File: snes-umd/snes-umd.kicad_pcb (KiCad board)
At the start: 2 copper layers, 2 parts

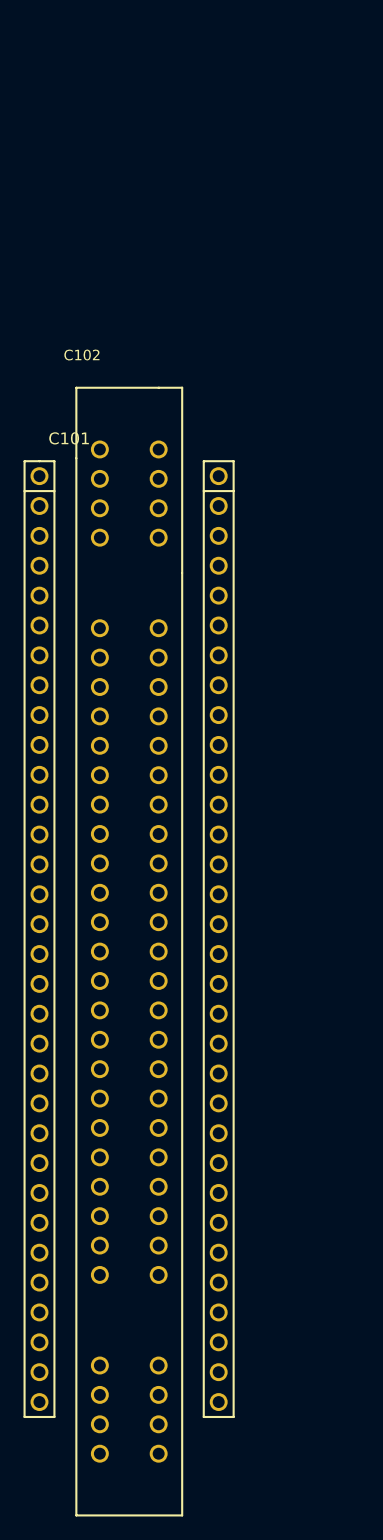
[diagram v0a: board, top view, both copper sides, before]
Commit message: finished schematic, board outline complete
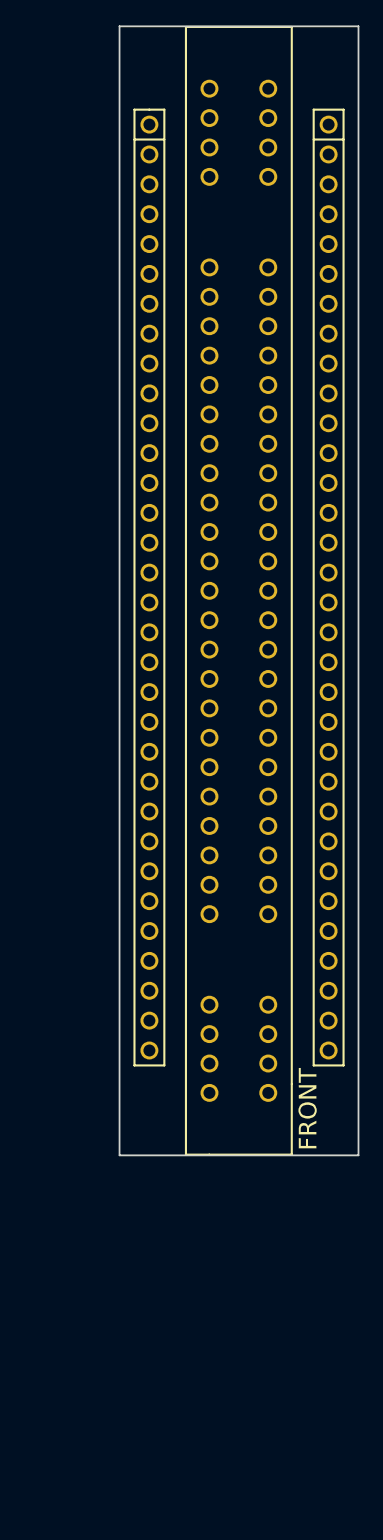
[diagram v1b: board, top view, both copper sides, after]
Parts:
- moved C102 56.6 mm to (143.2, 148.7), turned to 180 degrees
- moved C101 31.3 mm to (133.1, 66.4)
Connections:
- net Net-(C101-Pad12) renamed /D15
- net Net-(C101-Pad13) renamed /D14
- net Net-(C101-Pad16) renamed /D13
- net Net-(C101-Pad17) renamed /D12
- net Net-(C101-Pad48) renamed /D11
- net Net-(C101-Pad49) renamed /D10
- net Net-(C101-Pad52) renamed /D9
- net Net-(C101-Pad53) renamed /D8
- C101 pad 10: Net-(C101-Pad10) -> +5V
- C101 pad 11: Net-(C101-Pad11) -> /A15
- C101 pad 14: Net-(C101-Pad14) -> /A14
- C101 pad 15: Net-(C101-Pad15) -> /A13
- C101 pad 18: Net-(C101-Pad18) -> /A12
- C101 pad 19: Net-(C101-Pad19) -> /A7
- C101 pad 2: Net-(C101-Pad2) -> +5V
- C101 pad 20: Net-(C101-Pad20) -> /D7
- C101 pad 21: Net-(C101-Pad21) -> /D6
- C101 pad 22: Net-(C101-Pad22) -> /A6
- C101 pad 23: Net-(C101-Pad23) -> /A5
- C101 pad 24: Net-(C101-Pad24) -> /D5
- C101 pad 25: Net-(C101-Pad25) -> /D4
- C101 pad 26: Net-(C101-Pad26) -> /A4
- C101 pad 27: Net-(C101-Pad27) -> /A23
- C101 pad 28: Net-(C101-Pad28) -> /A22
- C101 pad 29: Net-(C101-Pad29) -> /A21
- C101 pad 30: Net-(C101-Pad30) -> /A20
- C101 pad 31: Net-(C101-Pad31) -> +5V
- C101 pad 34: Net-(C101-Pad34) -> +5V
- C101 pad 35: Net-(C101-Pad35) -> /A19
- C101 pad 36: Net-(C101-Pad36) -> /A18
- C101 pad 37: Net-(C101-Pad37) -> /A17
- C101 pad 38: Net-(C101-Pad38) -> /A16
- C101 pad 39: Net-(C101-Pad39) -> /A3
- C101 pad 40: Net-(C101-Pad40) -> /D3
- C101 pad 41: Net-(C101-Pad41) -> /D2
- C101 pad 42: Net-(C101-Pad42) -> /A2
- C101 pad 43: Net-(C101-Pad43) -> /A1
- C101 pad 44: Net-(C101-Pad44) -> /D1
- C101 pad 45: Net-(C101-Pad45) -> /D0
- C101 pad 46: Net-(C101-Pad46) -> /A0
- C101 pad 47: Net-(C101-Pad47) -> /A11
- C101 pad 50: Net-(C101-Pad50) -> /A10
- C101 pad 51: Net-(C101-Pad51) -> /A9
- C101 pad 54: Net-(C101-Pad54) -> /A8
- C101 pad 57: Net-(C101-Pad57) -> /~WR
- C101 pad 9: Net-(C101-Pad9) -> /~CE
- C102 pad 45: /~CART -> /~CE
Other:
- board outline added: 20.3 x 96 mm
- net class Default: clearance 0.2 -> 0.1778; trace_width 0.25 -> 0.1778; via_dia 0.6 -> 0.6096; via_drill 0.4 -> 0.3048
- net class Power added: clearance 0.1778, trace_width 0.3048, via_dia 0.6096, via_drill 0.3048
- rule trace_clearance: 0.2 -> 0.1778
- rule trace_min: 0.2 -> 0.1778
- rule via_min_drill: 0.3 -> 0.3048
- rule via_min_size: 0.4 -> 0.6096
- board text added: "FRONT"

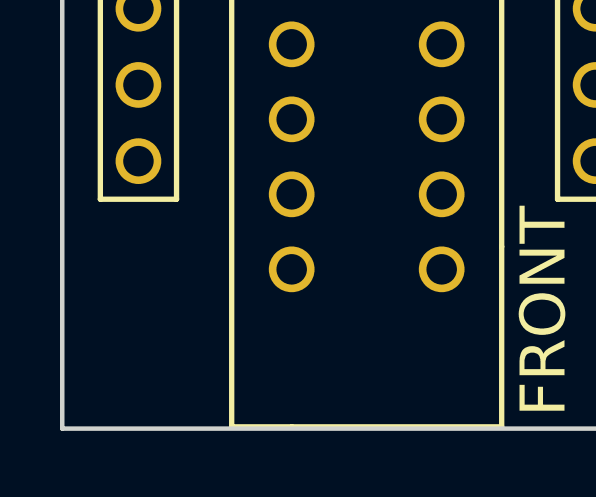
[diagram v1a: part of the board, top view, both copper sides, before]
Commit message: added db logo to PCB
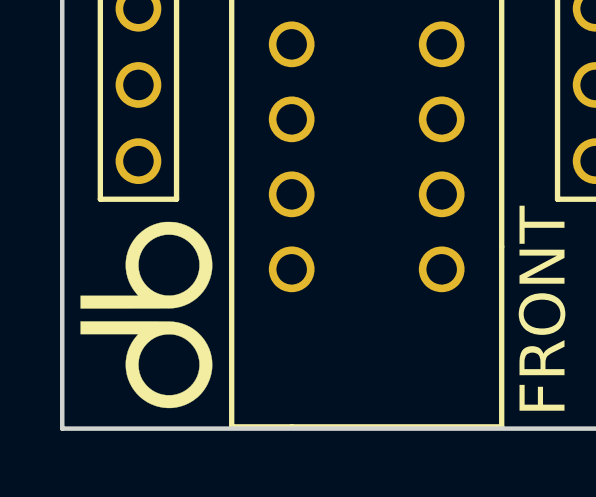
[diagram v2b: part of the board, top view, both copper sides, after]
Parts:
- added G***: LOGO, db-artwork:db-logo, F.Cu at (133.4, 150.3)
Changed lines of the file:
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@@
 (kicad_pcb (version 4) (host pcbnew 4.0.7-e2-6376~58~ubuntu16.04.1)
   (general
-    (links 46)
-    (no_connects 43)
-    (area 130.480999 52.9516 150.951001 154.257301)
+    (links 0)
+    (no_connects 46)
+    (area 130.480999 57.825179 150.951001 159.21978)
     (thickness 1.6)
     (drawings 5)
     (tracks 0)
     (zones 0)
-    (modules 2)
+    (modules 3)
     (nets 81)
   )
@@
       (net 36 "Net-(C102-Pad62)"))
   )
+  (module db-artwork:db-logo (layer F.Cu)
+    (at 133.35394 150.26688 90)
+    (fp_text reference G*** (at 0 0 90) (layer F.SilkS) hide
+      (effects (font (thickness 0.3)))
+    )
+    (fp_text value LOGO (at 0.75 0 90) (layer F.SilkS) hide
+      (effects (font (thickness 0.3)))
+    )
+    (fp_poly (pts (xy -0.211674 -0.696384) (xy -0.211728 -0.485513) (xy -0.211885 -0.288717) (xy -0.212146 -0.10623)
+      (xy -0.212509 0.061717) (xy -0.212971 0.21489) (xy -0.213533 0.353056) (xy -0.214193 0.475983)
+      (xy -0.214949 0.583437) (xy -0.2158 0.675185) (xy -0.216745 0.750995) (xy -0.217783 0.810634)
+      (xy -0.218912 0.853868) (xy -0.220131 0.880465) (xy -0.220476 0.884766) (xy -0.243499 1.042017)
+      (xy -0.282034 1.193165) (xy -0.335621 1.337431) (xy -0.4038 1.474037) (xy -0.48611 1.602203)
+      (xy -0.58209 1.721151) (xy -0.69128 1.830101) (xy -0.813219 1.928275) (xy -0.854272 1.956893)
+      (xy -0.987813 2.037224) (xy -1.125891 2.10136) (xy -1.269408 2.149644) (xy -1.419267 2.18242)
+      (xy -1.464547 2.189141) (xy -1.521839 2.194827) (xy -1.588776 2.19838) (xy -1.659761 2.199753)
+      (xy -1.7292 2.198903) (xy -1.791495 2.195782) (xy -1.8288 2.192102) (xy -1.978502 2.164772)
+      (xy -2.124359 2.122253) (xy -2.264749 2.065411) (xy -2.398053 1.99511) (xy -2.52265 1.912215)
+      (xy -2.63692 1.817591) (xy -2.739241 1.712103) (xy -2.748575 1.701202) (xy -2.84477 1.574991)
+      (xy -2.925819 1.442055) (xy -2.991529 1.303383) (xy -3.041705 1.159966) (xy -3.076153 1.012793)
+      (xy -3.094678 0.862854) (xy -3.095853 0.788868) (xy -2.674375 0.788868) (xy -2.664022 0.908167)
+      (xy -2.639427 1.026002) (xy -2.600489 1.14107) (xy -2.547108 1.252066) (xy -2.479182 1.357686)
+      (xy -2.396612 1.456625) (xy -2.375652 1.478185) (xy -2.277213 1.564994) (xy -2.17028 1.637625)
+      (xy -2.056166 1.695653) (xy -1.936181 1.738655) (xy -1.811637 1.766205) (xy -1.683844 1.777878)
+      (xy -1.554114 1.773251) (xy -1.490366 1.764925) (xy -1.367433 1.73671) (xy -1.249794 1.693424)
+      (xy -1.138765 1.636223) (xy -1.035664 1.566261) (xy -0.941807 1.484694) (xy -0.858511 1.392677)
+      (xy -0.787092 1.291365) (xy -0.728868 1.181913) (xy -0.685155 1.065478) (xy -0.682381 1.056091)
+      (xy -0.664575 0.990325) (xy -0.652432 0.933194) (xy -0.644996 0.878005) (xy -0.641313 0.818067)
+      (xy -0.640427 0.762) (xy -0.648 0.628662) (xy -0.671335 0.501448) (xy -0.710355 0.380547)
+      (xy -0.764986 0.266152) (xy -0.835151 0.158453) (xy -0.918482 0.060041) (xy -1.016343 -0.031031)
+      (xy -1.121621 -0.10693) (xy -1.233918 -0.167484) (xy -1.352838 -0.212525) (xy -1.477983 -0.24188)
+      (xy -1.608957 -0.255381) (xy -1.655234 -0.256329) (xy -1.787671 -0.248309) (xy -1.915004 -0.224398)
+      (xy -2.03654 -0.184821) (xy -2.151585 -0.129802) (xy -2.256602 -0.061682) (xy -2.356552 0.022367)
+      (xy -2.443067 0.115388) (xy -2.516046 0.216076) (xy -2.575389 0.323126) (xy -2.620994 0.435235)
+      (xy -2.65276 0.551098) (xy -2.670588 0.66941) (xy -2.674375 0.788868) (xy -3.095853 0.788868)
+      (xy -3.097088 0.711138) (xy -3.083186 0.558637) (xy -3.05278 0.406338) (xy -3.022763 0.303959)
+      (xy -2.96662 0.16067) (xy -2.896898 0.026545) (xy -2.814619 -0.097827) (xy -2.720806 -0.211859)
+      (xy -2.61648 -0.314961) (xy -2.502665 -0.406545) (xy -2.380383 -0.486023) (xy -2.250656 -0.552806)
+      (xy -2.114506 -0.606305) (xy -1.972957 -0.645931) (xy -1.827029 -0.671097) (xy -1.677746 -0.681214)
+      (xy -1.52613 -0.675693) (xy -1.373204 -0.653945) (xy -1.362507 -0.651806) (xy -1.220691 -0.614588)
+      (xy -1.08128 -0.561744) (xy -0.946864 -0.494582) (xy -0.82003 -0.414407) (xy -0.703368 -0.322527)
+      (xy -0.694154 -0.314355) (xy -0.635 -0.261393) (xy -0.635 -2.184401) (xy -0.211667 -2.184401)
+      (xy -0.211674 -0.696384)) (layer F.SilkS) (width 0.01))
+    (fp_poly (pts (xy 0.643466 -0.262528) (xy 0.719343 -0.32754) (xy 0.842777 -0.422731) (xy 0.972658 -0.50299)
+      (xy 1.10785 -0.568362) (xy 1.247218 -0.618891) (xy 1.389626 -0.654624) (xy 1.533939 -0.675606)
+      (xy 1.679021 -0.681883) (xy 1.823737 -0.6735) (xy 1.966951 -0.650502) (xy 2.107528 -0.612935)
+      (xy 2.244332 -0.560845) (xy 2.376229 -0.494277) (xy 2.502081 -0.413277) (xy 2.620754 -0.31789)
+      (xy 2.693256 -0.248449) (xy 2.796804 -0.131176) (xy 2.885375 -0.006823) (xy 2.959339 0.125347)
+      (xy 3.019066 0.266069) (xy 3.064927 0.416077) (xy 3.091639 0.541866) (xy 3.097294 0.587657)
+      (xy 3.100976 0.645953) (xy 3.102729 0.712446) (xy 3.102596 0.78283) (xy 3.100621 0.852796)
+      (xy 3.096849 0.918037) (xy 3.091324 0.974246) (xy 3.086922 1.003299) (xy 3.050466 1.158994)
+      (xy 2.999415 1.306132) (xy 2.933641 1.444959) (xy 2.853016 1.575722) (xy 2.757409 1.698668)
+      (xy 2.679479 1.782233) (xy 2.563048 1.886697) (xy 2.437715 1.97693) (xy 2.304273 2.052539)
+      (xy 2.163517 2.113132) (xy 2.016243 2.158316) (xy 1.863245 2.1877) (xy 1.855883 2.188692)
+      (xy 1.793422 2.194906) (xy 1.722251 2.198666) (xy 1.648096 2.199917) (xy 1.576681 2.198606)
+      (xy 1.513733 2.194679) (xy 1.490133 2.192102) (xy 1.337162 2.164131) (xy 1.189644 2.120699)
+      (xy 1.048628 2.062537) (xy 0.915165 1.990378) (xy 0.790305 1.904953) (xy 0.675097 1.806994)
+      (xy 0.570592 1.697234) (xy 0.47784 1.576403) (xy 0.397892 1.445236) (xy 0.385851 1.422355)
+      (xy 0.323052 1.284321) (xy 0.276045 1.144083) (xy 0.244 0.998763) (xy 0.228595 0.877107)
+      (xy 0.227548 0.856612) (xy 0.226557 0.819782) (xy 0.225626 0.767216) (xy 0.225335 0.744498)
+      (xy 0.646788 0.744498) (xy 0.652442 0.869944) (xy 0.673896 0.994598) (xy 0.711435 1.116968)
+      (xy 0.721701 1.142999) (xy 0.778365 1.259648) (xy 0.847839 1.366354) (xy 0.928867 1.46241)
+      (xy 1.020193 1.547108) (xy 1.120563 1.619741) (xy 1.22872 1.679602) (xy 1.343408 1.725982)
+      (xy 1.463373 1.758175) (xy 1.587358 1.775472) (xy 1.714109 1.777166) (xy 1.82602 1.765337)
+      (xy 1.95252 1.736494) (xy 2.072579 1.692605) (xy 2.185117 1.634685) (xy 2.289051 1.563752)
+      (xy 2.383299 1.480822) (xy 2.46678 1.386911) (xy 2.538412 1.283035) (xy 2.597112 1.170212)
+      (xy 2.6418 1.049458) (xy 2.659538 0.982133) (xy 2.672009 0.910004) (xy 2.679509 0.828786)
+      (xy 2.681825 0.744989) (xy 2.678745 0.665121) (xy 2.671823 0.605784) (xy 2.642687 0.477581)
+      (xy 2.599484 0.357488) (xy 2.543325 0.24614) (xy 2.475321 0.144174) (xy 2.396582 0.052227)
+      (xy 2.308218 -0.029065) (xy 2.21134 -0.099066) (xy 2.10706 -0.157138) (xy 1.996487 -0.202646)
+      (xy 1.880733 -0.234952) (xy 1.760907 -0.253421) (xy 1.638121 -0.257415) (xy 1.513485 -0.246298)
+      (xy 1.38811 -0.219434) (xy 1.289194 -0.186629) (xy 1.18186 -0.136649) (xy 1.078446 -0.071497)
+      (xy 0.981455 0.007125) (xy 0.928723 0.05865) (xy 0.845554 0.15755) (xy 0.776478 0.264601)
+      (xy 0.721778 0.378311) (xy 0.681741 0.497191) (xy 0.656649 0.61975) (xy 0.646788 0.744498)
+      (xy 0.225335 0.744498) (xy 0.224757 0.69951) (xy 0.223954 0.617264) (xy 0.22322 0.521076)
+      (xy 0.222558 0.411543) (xy 0.221971 0.289264) (xy 0.221463 0.154837) (xy 0.221036 0.00886)
+      (xy 0.220694 -0.148068) (xy 0.220439 -0.31535) (xy 0.220276 -0.492388) (xy 0.220207 -0.678582)
+      (xy 0.220206 -0.700617) (xy 0.220133 -2.184401) (xy 0.643466 -2.184401) (xy 0.643466 -0.262528)) (layer F.SilkS) (width 0.01))
+  )
   (gr_text FRONT (at 146.60394 150.14188 90) (layer F.SilkS)

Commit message: routing the pcb, learning KiCad
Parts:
- moved G*** 0.16 mm to (133.3, 150.4)
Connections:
- C101 pad 1: GND -> (no net)
- C101 pad 10: +5V -> (no net)
- C101 pad 12: /D15 -> (no net)
- C101 pad 13: /D14 -> (no net)
- C101 pad 16: /D13 -> (no net)
- C101 pad 17: /D12 -> (no net)
- C101 pad 3: Net-(C101-Pad3) -> (no net)
- C101 pad 31: +5V -> (no net)
- C101 pad 34: +5V -> (no net)
- C101 pad 4: Net-(C101-Pad4) -> (no net)
- C101 pad 48: /D11 -> (no net)
- C101 pad 49: /D10 -> (no net)
- C101 pad 5: Net-(C101-Pad5) -> (no net)
- C101 pad 52: /D9 -> (no net)
- C101 pad 53: /D8 -> (no net)
- C101 pad 55: GND -> (no net)
- C101 pad 56: Net-(C101-Pad56) -> (no net)
- C101 pad 58: Net-(C101-Pad58) -> /~RESET
- C101 pad 59: Net-(C101-Pad59) -> (no net)
- C101 pad 6: Net-(C101-Pad6) -> (no net)
- C101 pad 60: Net-(C101-Pad60) -> (no net)
- C101 pad 61: Net-(C101-Pad61) -> (no net)
- C101 pad 62: Net-(C101-Pad62) -> (no net)
- C101 pad 63: Net-(C101-Pad63) -> (no net)
- C101 pad 64: GND -> (no net)
- C101 pad 7: Net-(C101-Pad7) -> (no net)
- C102 pad 1: Net-(C102-Pad1) -> (no net)
- C102 pad 18: Net-(C102-Pad18) -> (no net)
- C102 pad 2: Net-(C102-Pad2) -> (no net)
- C102 pad 24: Net-(C102-Pad24) -> (no net)
- C102 pad 25: Net-(C102-Pad25) -> (no net)
- C102 pad 28: Net-(C102-Pad28) -> (no net)
- C102 pad 29: Net-(C102-Pad29) -> (no net)
- C102 pad 3: Net-(C102-Pad3) -> (no net)
- C102 pad 30: Net-(C102-Pad30) -> (no net)
- C102 pad 31: Net-(C102-Pad31) -> (no net)
- C102 pad 32: Net-(C102-Pad32) -> (no net)
- C102 pad 33: Net-(C102-Pad33) -> (no net)
- C102 pad 34: Net-(C102-Pad34) -> (no net)
- C102 pad 35: Net-(C102-Pad35) -> (no net)
- C102 pad 37: Net-(C102-Pad37) -> (no net)
- C102 pad 38: Net-(C102-Pad38) -> (no net)
- C102 pad 39: Net-(C102-Pad39) -> (no net)
- C102 pad 4: Net-(C102-Pad4) -> (no net)
- C102 pad 59: Net-(C102-Pad59) -> (no net)
- C102 pad 60: Net-(C102-Pad60) -> (no net)
- C102 pad 61: Net-(C102-Pad61) -> (no net)
- C102 pad 62: Net-(C102-Pad62) -> (no net)
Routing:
- net /D3: track 0.00 -> 43.5 mm
- net /D2: track 0.00 -> 35.7 mm
- net GND: track 0.00 -> 32.4 mm
- net /D1: track 0.00 -> 27.7 mm
- net /A4: track 0.00 -> 25.7 mm, vias 0 -> 1
- net /D0: track 0.00 -> 21.1 mm
- net /A3: track 0.00 -> 21.0 mm
- net /A7: track 0.00 -> 20.4 mm
- net /~CE: track 0.00 -> 19.1 mm
- net /A16: track 0.00 -> 18.4 mm
- net /A1: track 0.00 -> 17.2 mm
- net /A2: track 0.00 -> 17.2 mm
- net +5V: track 0.00 -> 16.7 mm
- net /~RD: track 0.00 -> 13.4 mm
- net /A6: track 0.00 -> 12.7 mm, vias 0 -> 1
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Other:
- rule pad_to_mask_clearance: 0.2 -> 0.1016

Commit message: more routing work
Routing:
- net /A8: track 0.00 -> 35.2 mm
- net /A23: track 0.00 -> 33.6 mm, vias 0 -> 1
- net /A13: track 0.00 -> 33.3 mm
- net /A21: track 0.00 -> 33.2 mm, vias 0 -> 1
- net /D5: track 0.00 -> 32.2 mm
- net /A22: track 0.00 -> 31.7 mm, vias 0 -> 1
- net /A20: track 0.00 -> 31.4 mm, vias 0 -> 1
- net /A14: track 0.00 -> 31.0 mm
- net /D4: track 0.00 -> 30.9 mm, vias 0 -> 1
- net /A10: track 0.00 -> 29.5 mm
- net /A9: track 0.00 -> 29.5 mm
- net /D6: track 0.00 -> 25.8 mm
- net /D7: track 0.00 -> 25.7 mm
- net /A12: track 0.00 -> 24.9 mm
- net /A11: track 0.00 -> 23.6 mm
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
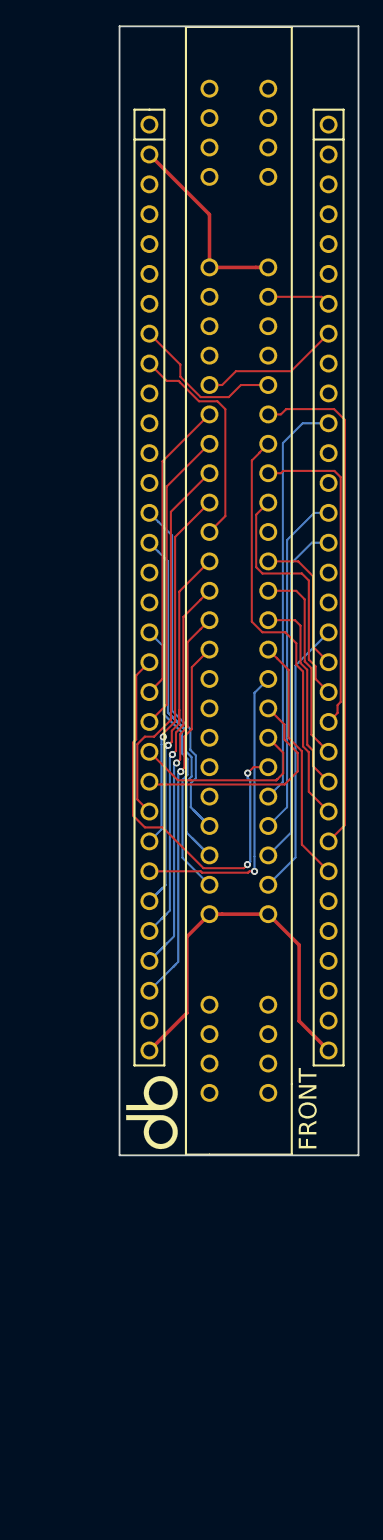
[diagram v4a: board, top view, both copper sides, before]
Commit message: first pass routing complete on SNES adapter
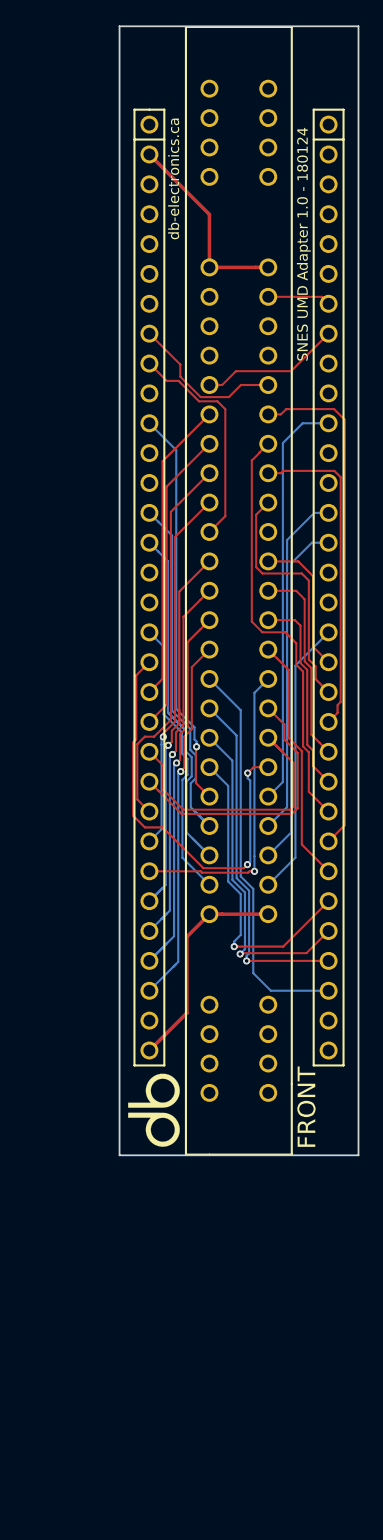
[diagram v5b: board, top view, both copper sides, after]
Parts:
- moved G*** 0.26 mm to (133.5, 150.2)
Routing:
- net /A15: track 0.00 -> 33.9 mm, vias 0 -> 1
- net /A19: track 0.00 -> 33.6 mm
- net /A18: track 0.00 -> 29.9 mm, vias 0 -> 1
- net /A17: track 0.00 -> 28.1 mm, vias 0 -> 1
- net /A16: track 0.00 -> 26.2 mm, vias 0 -> 1
- net GND: track 32.4 -> 18.7 mm
- net /A6: track 16.4 -> 24.1 mm
- net /A5: track 19.6 -> 23.5 mm
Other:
- board text added: "SNES UMD Adapter 1.0 - 180124"
- board text added: "db-electronics.ca"
